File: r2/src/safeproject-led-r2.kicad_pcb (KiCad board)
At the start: 2 copper layers, 29 x 51.5 mm, 21 parts, among them J1 2842142-4, J2 Conn_01x20

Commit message: Remove copper and mask around mounting holes
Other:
- board text added: "safeacoustics-led-r2 Monad 2021"
- board text removed: "safeacoustics-led-r1 Monad 2021"

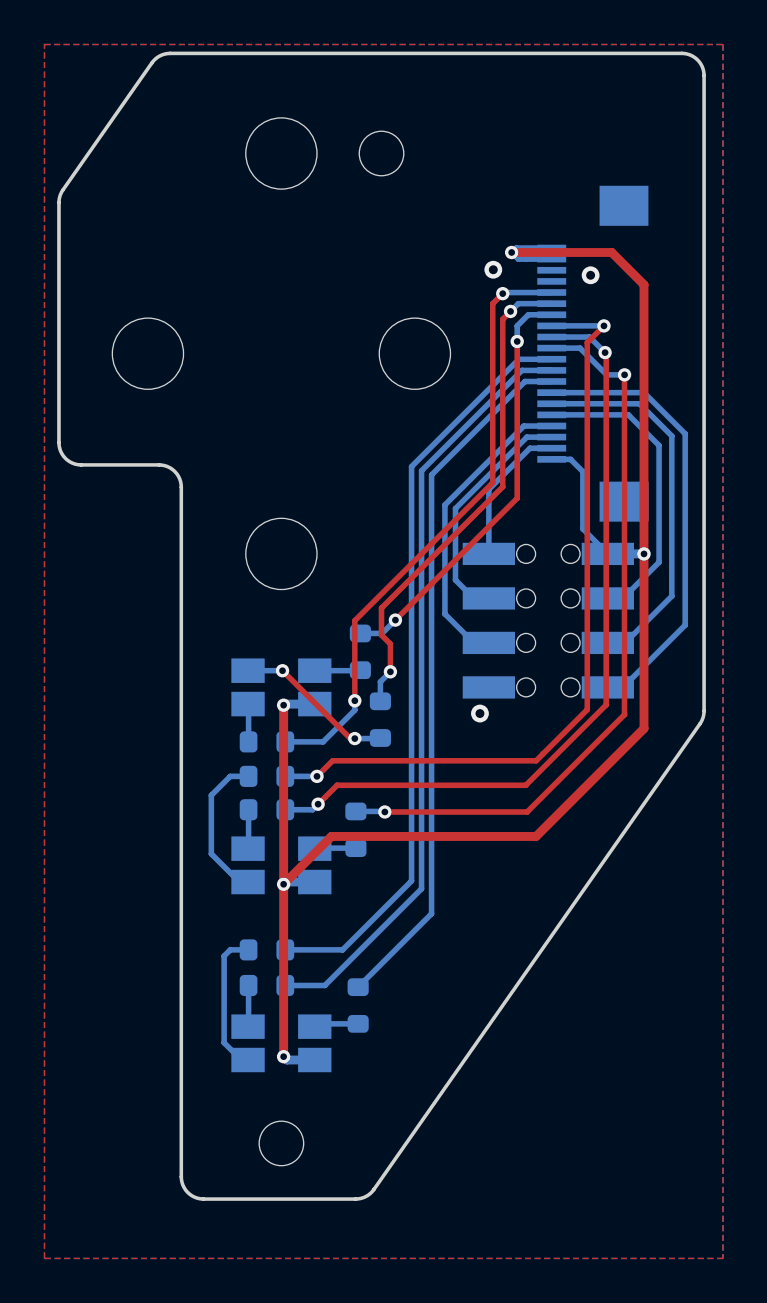
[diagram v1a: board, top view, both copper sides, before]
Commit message: Rewire the board to use the new 5V line on FFC pin 20 for the LED power. Prevents us injecting LED switching noise into the 3V3 rail
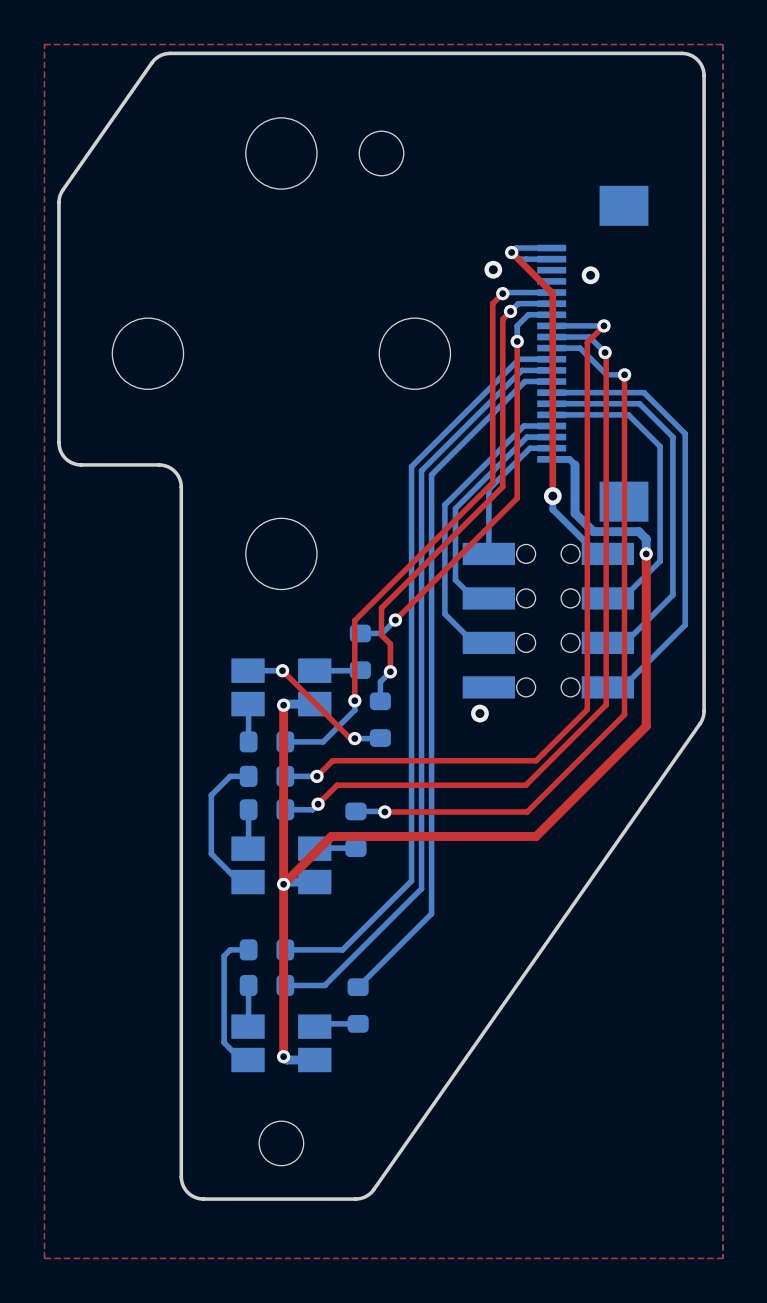
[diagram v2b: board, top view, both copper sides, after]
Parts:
- removed the REF** at (0.00, 35.5)
- removed the REF** at (-6.00, 0.00)
- removed the REF** at (4.50, -9.00)
- added ?: , , F.Cu at (4.50, -9.00)
- added ?: , , F.Cu at (0.00, 35.5)
- J2: value Conn_01x20 -> FH12-20S-0.5SH
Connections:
- J2 pad 20: +3V3 -> +5V
- LED1 pad 2: +3V3 -> +5V
- LED2 pad 2: +3V3 -> +5V
- LED3 pad 2: +3V3 -> +5V
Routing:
- net +3V3: track 77.0 -> 19.4 mm, vias 5 -> 2
- net +5V: track 0.00 -> 54.8 mm, vias 0 -> 4
